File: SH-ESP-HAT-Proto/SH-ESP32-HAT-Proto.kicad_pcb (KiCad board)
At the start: 2 copper layers, 83 x 55.5 mm, 465 parts, among them J301 Conn_01x02, J302 GPIO, J303 I2C, J304 Conn_01x02, J305 I2C, J306 Conn_01x04, J307 GPIO, P301 Conn_01x01_Male, P302 Conn_01x01_Male, P303 Conn_01x01_Male, P304 Conn_01x01_Male, P305 Conn_01x01_Male, P306 Conn_01x01_Male, P307 Conn_01x01_Male, P308 Conn_01x01_Male, P309 Conn_01x01_Male, P310 Conn_01x01_Male, P311 Conn_01x01_Male, P312 Conn_01x01_Male, P313 Conn_01x01_Male, P314 Conn_01x01_Male, P315 Conn_01x01_Male, P316 Conn_01x01_Male, P317 Conn_01x01_Male, P318 Conn_01x01_Male, P319 Conn_01x01_Male, P320 Conn_01x01_Male, P321 Conn_01x01_Male, P331 Conn_01x01_Male

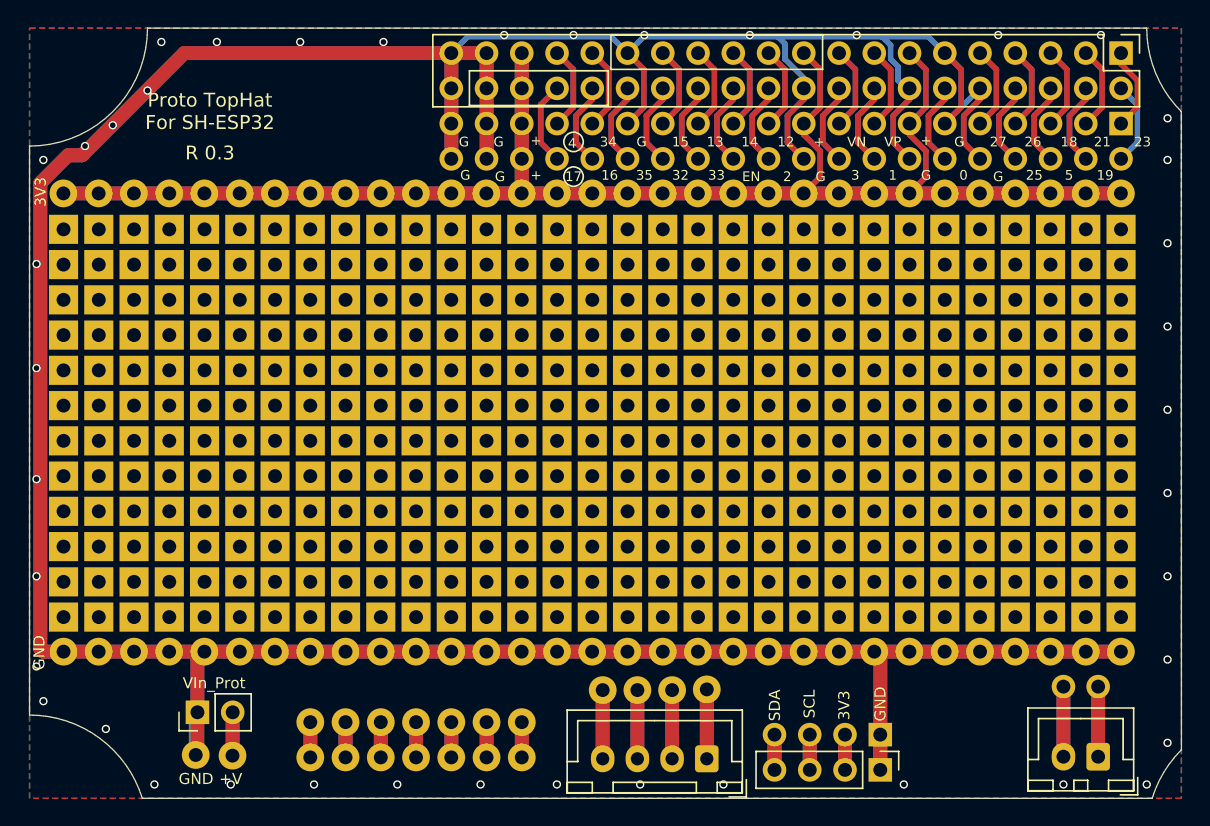
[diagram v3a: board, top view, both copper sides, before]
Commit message: Update the proto top hat design
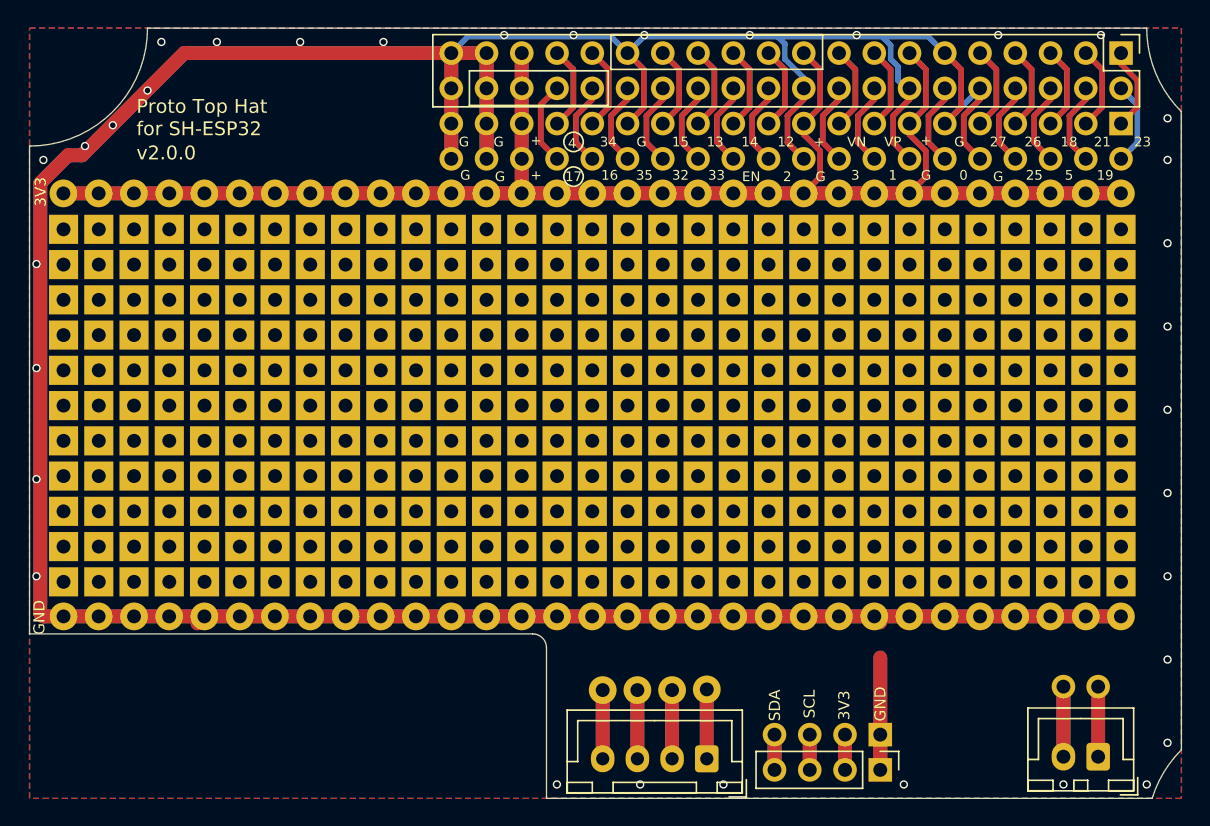
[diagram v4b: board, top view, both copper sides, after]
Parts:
- removed J304: Conn_01x02, Connector_PinHeader_2.54mm:PinHeader_1x02_P2.54mm_Vertical
- removed P307, P308, P309, P310, P311, P312, P313, P314, P315, P316, P317, P318, P319, P320, P321, P331: Conn_01x01_Male, ESP32-HAT:ProtoPad-Drill1mm
- removed the REF** at (147.3, 99.4)
- removed the REF** at (144.8, 99.4)
- removed the REF** at (142.2, 99.4)
- removed the REF** at (137.2, 99.4)
- removed the REF** at (165.1, 99.4)
- removed the REF** at (139.7, 99.4)
- removed the REF** at (132.1, 99.4)
- removed the REF** at (134.6, 99.4)
- removed the REF** at (129.6, 99.4)
- removed the REF** at (127.0, 99.4)
- removed the REF** at (121.9, 99.4)
- removed the REF** at (124.5, 99.4)
- removed the REF** at (116.8, 99.4)
- removed the REF** at (119.4, 99.4)
- removed the REF** at (114.3, 99.4)
- removed the REF** at (111.8, 99.4)
- removed the REF** at (109.2, 99.4)
- removed the REF** at (106.7, 99.4)
- removed the REF** at (167.7, 99.4)
- removed the REF** at (101.6, 99.4)
- removed the REF** at (104.2, 99.4)
- removed the REF** at (99.1, 99.4)
- removed the REF** at (96.5, 99.4)
- removed the REF** at (94.0, 99.4)
- removed the REF** at (162.6, 99.4)
- removed the REF** at (91.5, 99.4)
- removed the REF** at (157.5, 99.4)
- removed the REF** at (160.0, 99.4)
- removed the REF** at (154.9, 99.4)
- removed the REF** at (152.4, 99.4)
- removed the REF** at (149.9, 99.4)
- moved REF** 2.54 mm to (119.4, 99.4)
- moved REF** 2.54 mm to (116.8, 99.4)
- moved REF** 2.54 mm to (114.3, 99.4)
- moved REF** 2.54 mm to (111.8, 99.4)
- moved REF** 2.54 mm to (109.2, 99.4)
- moved REF** 2.54 mm to (106.7, 99.4)
- moved REF** 2.54 mm to (101.6, 99.4)
- moved REF** 2.54 mm to (99.1, 99.4)
- moved REF** 2.54 mm to (104.2, 99.4)
- moved REF** 2.54 mm to (96.5, 99.4)
- moved REF** 2.54 mm to (139.7, 99.4)
- moved REF** 2.54 mm to (137.2, 99.4)
- moved REF** 2.54 mm to (142.2, 99.4)
- moved REF** 2.54 mm to (149.9, 99.4)
- moved REF** 2.54 mm to (147.3, 99.4)
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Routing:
- net GND: track 472.5 -> 453.4 mm, vias 42 -> 34
- net /IOHeader/Vin_protected: track 6.26 -> 0.00 mm
- net Net-(P313-Pad1): track 5.08 -> 0.00 mm
- net Net-(P312-Pad1): track 5.08 -> 0.00 mm
- net Net-(P311-Pad1): track 5.08 -> 0.00 mm
- net Net-(P310-Pad1): track 5.08 -> 0.00 mm
- net Net-(P309-Pad1): track 5.08 -> 0.00 mm
- net Net-(P308-Pad1): track 5.08 -> 0.00 mm
- net Net-(P307-Pad1): track 5.08 -> 0.00 mm
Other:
- outline, holes or cut-outs redrawn
- net class Default removed
- board text added: "Proto Top Hat for SH-ESP32"
- board text added: "v2.0.0"
- board text removed: "+V"
- board text removed: "Proto TopHat For SH-ESP32"
- board text removed: "R 0.3"
- board text removed: "VIn_Prot"
